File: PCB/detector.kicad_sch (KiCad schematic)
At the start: 13 parts, among them J6 Audio In, J7 Through, U2 TL072, U3 LM393

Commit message: fix schematics after further testing
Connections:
- net at R23.2, U2.1, U2.2 (-): now also U3.2 (-), U3.5 (+); no longer U3.3 (+), U3.6 (_)
- net at R20.1: now also U3.3 (+); no longer U3.2 (-)
- net at R22.1, U2.7: now also U3.6 (_); no longer U3.5 (+)
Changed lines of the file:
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@@
+    (stroke (width 0) (type default))
+  )
+  (wire (pts (xy 154.94 52.07) (xy 182.88 52.07))
+    (stroke (width 0) (type default))
+  )
+  (wire (pts (xy 24.13 185.42) (xy 38.1 185.42))
+    (stroke (width 0) (type default))
+  )
+  (wire (pts (xy 181.61 82.55) (xy 182.88 82.55))
+    (stroke (width 0) (type default))
+  )
+  (wire (pts (xy 171.45 80.01) (xy 173.99 80.01))
+    (stroke (width 0) (type default))
+  )
+  (wire (pts (xy 123.19 68.58) (xy 123.19 116.84))
+    (stroke (width 0) (type default))
+  )
+  (wire (pts (xy 38.1 166.37) (xy 38.1 170.18))
+    (stroke (width 0) (type default))
+  )
+  (wire (pts (xy 54.61 170.18) (xy 54.61 175.26))
+    (stroke (width 0) (type default))
+  )
+  (wire (pts (xy 67.31 52.07) (xy 143.51 52.07))
+    (stroke (width 0) (type default))
+  )
+  (wire (pts (xy 181.61 57.15) (xy 181.61 68.58))
+    (stroke (width 0) (type default))
+  )
+  (wire (pts (xy 154.94 85.09) (xy 158.75 85.09))
+    (stroke (width 0) (type default))
+  )
+  (wire (pts (xy 54.61 156.21) (xy 54.61 158.75))
+    (stroke (width 0) (type default))
+  )
+  (wire (pts (xy 163.83 80.01) (xy 158.75 80.01))
+    (stroke (width 0) (type default))
+  )
+  (wire (pts (xy 43.18 177.8) (xy 43.18 185.42))
+    (stroke (width 0) (type default))
+  )
+  (wire (pts (xy 68.58 66.04) (xy 76.2 66.04))
+    (stroke (width 0) (type default))
+  )
+  (wire (pts (xy 198.12 68.58) (xy 198.12 85.09))
+    (stroke (width 0) (type default))
+  )
+  (wire (pts (xy 158.75 90.17) (xy 158.75 92.71))
+    (stroke (width 0) (type default))
+  )
+  (wire (pts (xy 181.61 68.58) (xy 181.61 82.55))
+    (stroke (width 0) (type default))
+  )
+  (wire (pts (xy 38.1 156.21) (xy 38.1 158.75))
+    (stroke (width 0) (type default))
+  )
+  (wire (pts (xy 24.13 156.21) (xy 38.1 156.21))
+    (stroke (width 0) (type default))
+  )
+  (wire (pts (xy 207.01 68.58) (xy 198.12 68.58))
+    (stroke (width 0) (type default))
+  )
+  (wire (pts (xy 201.93 119.38) (xy 201.93 121.92))
+    (stroke (width 0) (type default))
+  )
+  (wire (pts (xy 71.12 68.58) (xy 71.12 71.12))
+    (stroke (width 0) (type default))
+  )
+  (wire (pts (xy 59.69 185.42) (xy 54.61 185.42))
+    (stroke (width 0) (type default))
+  )
+  (wire (pts (xy 38.1 170.18) (xy 54.61 170.18))
+    (stroke (width 0) (type default))
+  )
+  (wire (pts (xy 38.1 182.88) (xy 38.1 185.42))
+    (stroke (width 0) (type default))
+  )
+  (wire (pts (xy 43.18 156.21) (xy 43.18 162.56))
+    (stroke (width 0) (type default))
+  )
+  (wire (pts (xy 68.58 63.5) (xy 71.12 63.5))
+    (stroke (width 0) (type default))
+  )
+  (wire (pts (xy 99.06 76.2) (xy 83.82 76.2))
+    (stroke (width 0) (type default))
+  )
+  (wire (pts (xy 173.99 87.63) (xy 182.88 87.63))
+    (stroke (width 0) (type default))
+  )
+  (wire (pts (xy 182.88 57.15) (xy 181.61 57.15))
+    (stroke (width 0) (type default))
+  )
+  (wire (pts (xy 43.18 185.42) (xy 38.1 185.42))
+    (stroke (width 0) (type default))
+  )
+  (wire (pts (xy 123.19 68.58) (xy 181.61 68.58))
+    (stroke (width 0) (type default))
+  )
+  (wire (pts (xy 54.61 182.88) (xy 54.61 185.42))
+    (stroke (width 0) (type default))
+  )
+  (wire (pts (xy 38.1 170.18) (xy 38.1 175.26))
+    (stroke (width 0) (type default))
+  )
+  (wire (pts (xy 158.75 80.01) (xy 158.75 85.09))
+    (stroke (width 0) (type default))
+  )
+  (wire (pts (xy 143.51 52.07) (xy 147.32 52.07))
+    (stroke (width 0) (type default))
+  )
+  (wire (pts (xy 38.1 156.21) (xy 43.18 156.21))
     (stroke (width 0) (type default))
   )
   (wire (pts (xy 198.12 54.61) (xy 198.12 68.58))
-    (stroke (width 0) (type default))
-  )
-  (wire (pts (xy 154.94 52.07) (xy 182.88 52.07))
-    (stroke (width 0) (type default))
-  )
-  (wire (pts (xy 24.13 185.42) (xy 38.1 185.42))
-    (stroke (width 0) (type default))
-  )
-  (wire (pts (xy 181.61 82.55) (xy 182.88 82.55))
-    (stroke (width 0) (type default))
-  )
-  (wire (pts (xy 171.45 80.01) (xy 173.99 80.01))
-    (stroke (width 0) (type default))
-  )
-  (wire (pts (xy 123.19 68.58) (xy 123.19 116.84))
-    (stroke (width 0) (type default))
-  )
-  (wire (pts (xy 38.1 166.37) (xy 38.1 170.18))
-    (stroke (width 0) (type default))
-  )
-  (wire (pts (xy 54.61 170.18) (xy 54.61 175.26))
-    (stroke (width 0) (type default))
-  )
-  (wire (pts (xy 67.31 52.07) (xy 143.51 52.07))
-    (stroke (width 0) (type default))
-  )
-  (wire (pts (xy 181.61 57.15) (xy 181.61 68.58))
-    (stroke (width 0) (type default))
-  )
-  (wire (pts (xy 154.94 85.09) (xy 158.75 85.09))
-    (stroke (width 0) (type default))
-  )
-  (wire (pts (xy 54.61 156.21) (xy 54.61 158.75))
-    (stroke (width 0) (type default))
-  )
-  (wire (pts (xy 163.83 80.01) (xy 158.75 80.01))
-    (stroke (width 0) (type default))
-  )
-  (wire (pts (xy 43.18 177.8) (xy 43.18 185.42))
-    (stroke (width 0) (type default))
-  )
-  (wire (pts (xy 68.58 66.04) (xy 76.2 66.04))
-    (stroke (width 0) (type default))
-  )
-  (wire (pts (xy 198.12 68.58) (xy 198.12 85.09))
-    (stroke (width 0) (type default))
-  )
-  (wire (pts (xy 158.75 90.17) (xy 158.75 92.71))
-    (stroke (width 0) (type default))
-  )
-  (wire (pts (xy 181.61 68.58) (xy 181.61 82.55))
-    (stroke (width 0) (type default))
-  )
-  (wire (pts (xy 38.1 156.21) (xy 38.1 158.75))
-    (stroke (width 0) (type default))
-  )
-  (wire (pts (xy 24.13 156.21) (xy 38.1 156.21))
-    (stroke (width 0) (type default))
-  )
-  (wire (pts (xy 207.01 68.58) (xy 198.12 68.58))
-    (stroke (width 0) (type default))
-  )
-  (wire (pts (xy 201.93 119.38) (xy 201.93 121.92))
-    (stroke (width 0) (type default))
-  )
-  (wire (pts (xy 71.12 68.58) (xy 71.12 71.12))
-    (stroke (width 0) (type default))
-  )
-  (wire (pts (xy 59.69 185.42) (xy 54.61 185.42))
-    (stroke (width 0) (type default))
-  )
-  (wire (pts (xy 38.1 170.18) (xy 54.61 170.18))
-    (stroke (width 0) (type default))
-  )
-  (wire (pts (xy 38.1 182.88) (xy 38.1 185.42))
-    (stroke (width 0) (type default))
-  )
-  (wire (pts (xy 43.18 156.21) (xy 43.18 162.56))
-    (stroke (width 0) (type default))
-  )
-  (wire (pts (xy 68.58 63.5) (xy 71.12 63.5))
-    (stroke (width 0) (type default))
-  )
-  (wire (pts (xy 99.06 76.2) (xy 83.82 76.2))
-    (stroke (width 0) (type default))
-  )
-  (wire (pts (xy 173.99 87.63) (xy 182.88 87.63))
-    (stroke (width 0) (type default))
-  )
-  (wire (pts (xy 182.88 57.15) (xy 181.61 57.15))
-    (stroke (width 0) (type default))
-  )
-  (wire (pts (xy 43.18 185.42) (xy 38.1 185.42))
-    (stroke (width 0) (type default))
-  )
-  (wire (pts (xy 123.19 68.58) (xy 181.61 68.58))
-    (stroke (width 0) (type default))
-  )
-  (wire (pts (xy 54.61 182.88) (xy 54.61 185.42))
-    (stroke (width 0) (type default))
-  )
-  (wire (pts (xy 38.1 170.18) (xy 38.1 175.26))
-    (stroke (width 0) (type default))
-  )
-  (wire (pts (xy 158.75 80.01) (xy 158.75 85.09))
-    (stroke (width 0) (type default))
-  )
-  (wire (pts (xy 143.51 52.07) (xy 147.32 52.07))
-    (stroke (width 0) (type default))
-  )
-  (wire (pts (xy 38.1 156.21) (xy 43.18 156.21))
     (stroke (width 0) (type default))
   )
@@
     )
   )
-  (symbol (lib_id "Comparator:LM393") (at 190.5 54.61 0) (mirror x) (unit 1)
+  (symbol (lib_id "Comparator:LM393") (at 190.5 54.61 0) (unit 1)
     (in_bom yes) (on_board yes) (dnp no)
-    (property "Reference" "U3" (at 190.5 44.45 0)
-      (effects (font (size 1.27 1.27)))
-    )
-    (property "Value" "LM393" (at 190.5 46.99 0)
+    (property "Reference" "U3" (at 190.5 64.77 0)
+      (effects (font (size 1.27 1.27)))
+    )
+    (property "Value" "LM393" (at 190.5 62.23 0)
       (effects (font (size 1.27 1.27)))
     )
@@
     )
   )
-  (symbol (lib_id "Comparator:LM393") (at 190.5 85.09 0) (mirror x) (unit 2)
+  (symbol (lib_id "Comparator:LM393") (at 190.5 85.09 0) (unit 2)
     (in_bom yes) (on_board yes) (dnp no)
-    (property "Reference" "U3" (at 190.5 92.71 0)
-      (effects (font (size 1.27 1.27)))
-    )
-    (property "Value" "LM393" (at 190.5 95.25 0)
-      (effects (font (size 1.27 1.27)))
-    )
+    (property "Reference" "U3" (at 190.5 77.47 0)
+      (effects (font (size 1.27 1.27)))
+    )
+    (property "Value" "LM393" (at 190.5 74.93 0)
+      (effects (font (size 1.27 1.27)))
+    )

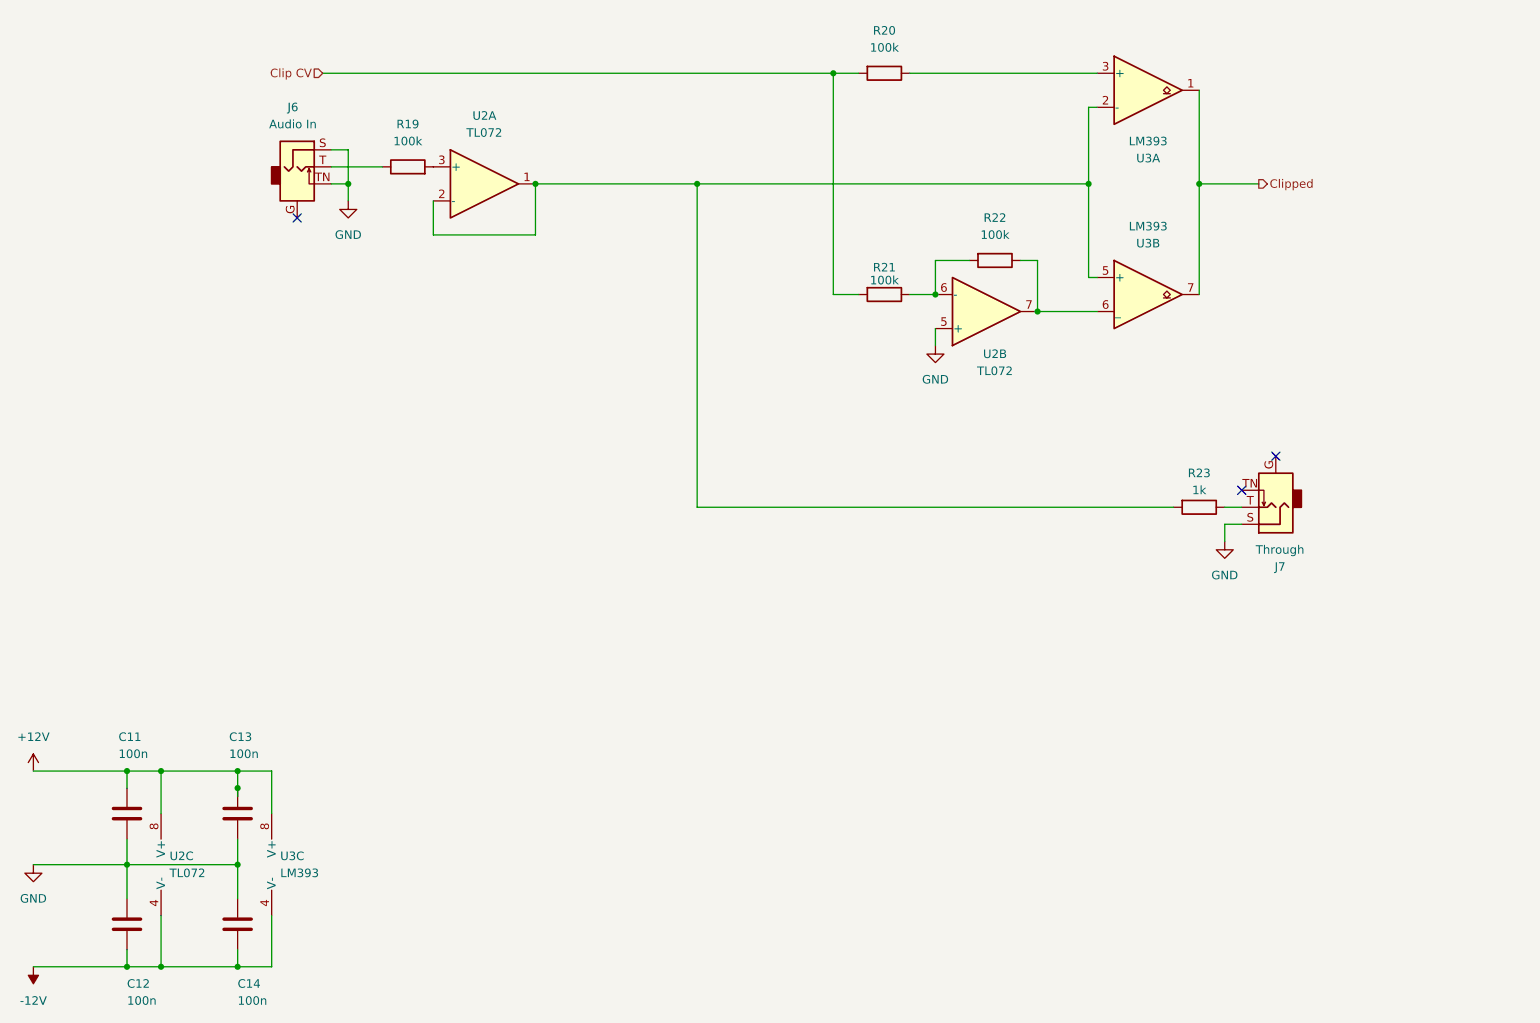
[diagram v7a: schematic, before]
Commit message: :art: Apply geographical reannotation
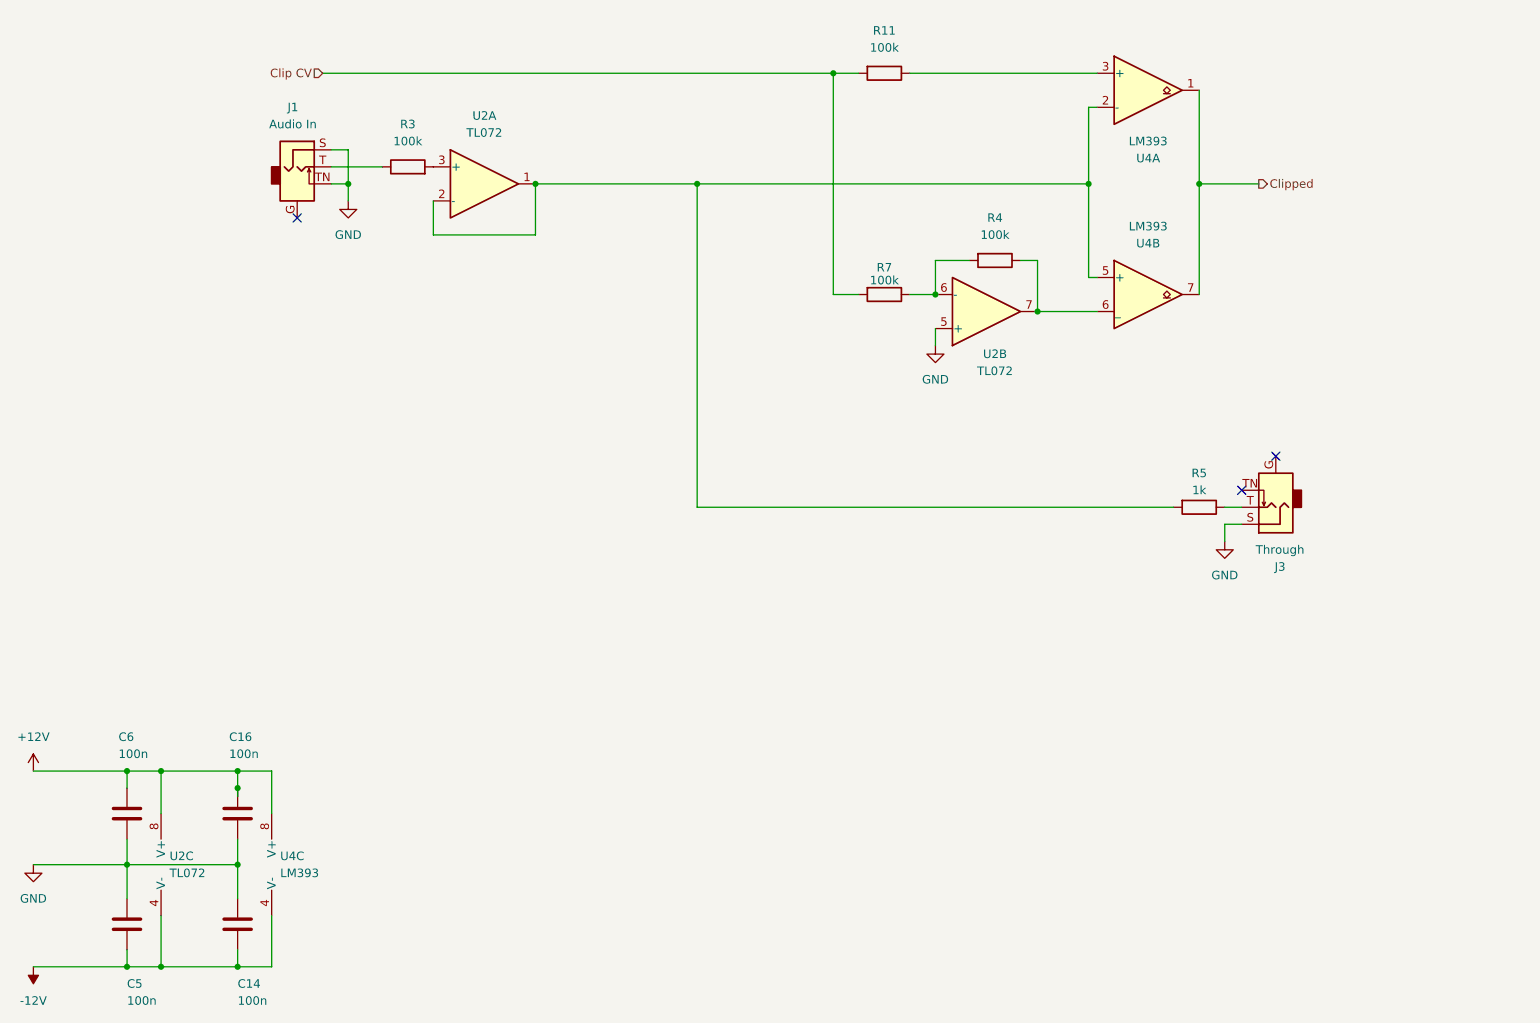
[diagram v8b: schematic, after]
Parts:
- renumbered C13 to C16, C12 to C5, C11 to C6, J6 to J1, J7 to J3, R20 to R11, R19 to R3, R22 to R4, R23 to R5, R21 to R7, U3 to U4
